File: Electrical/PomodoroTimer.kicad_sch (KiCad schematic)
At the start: 1 part

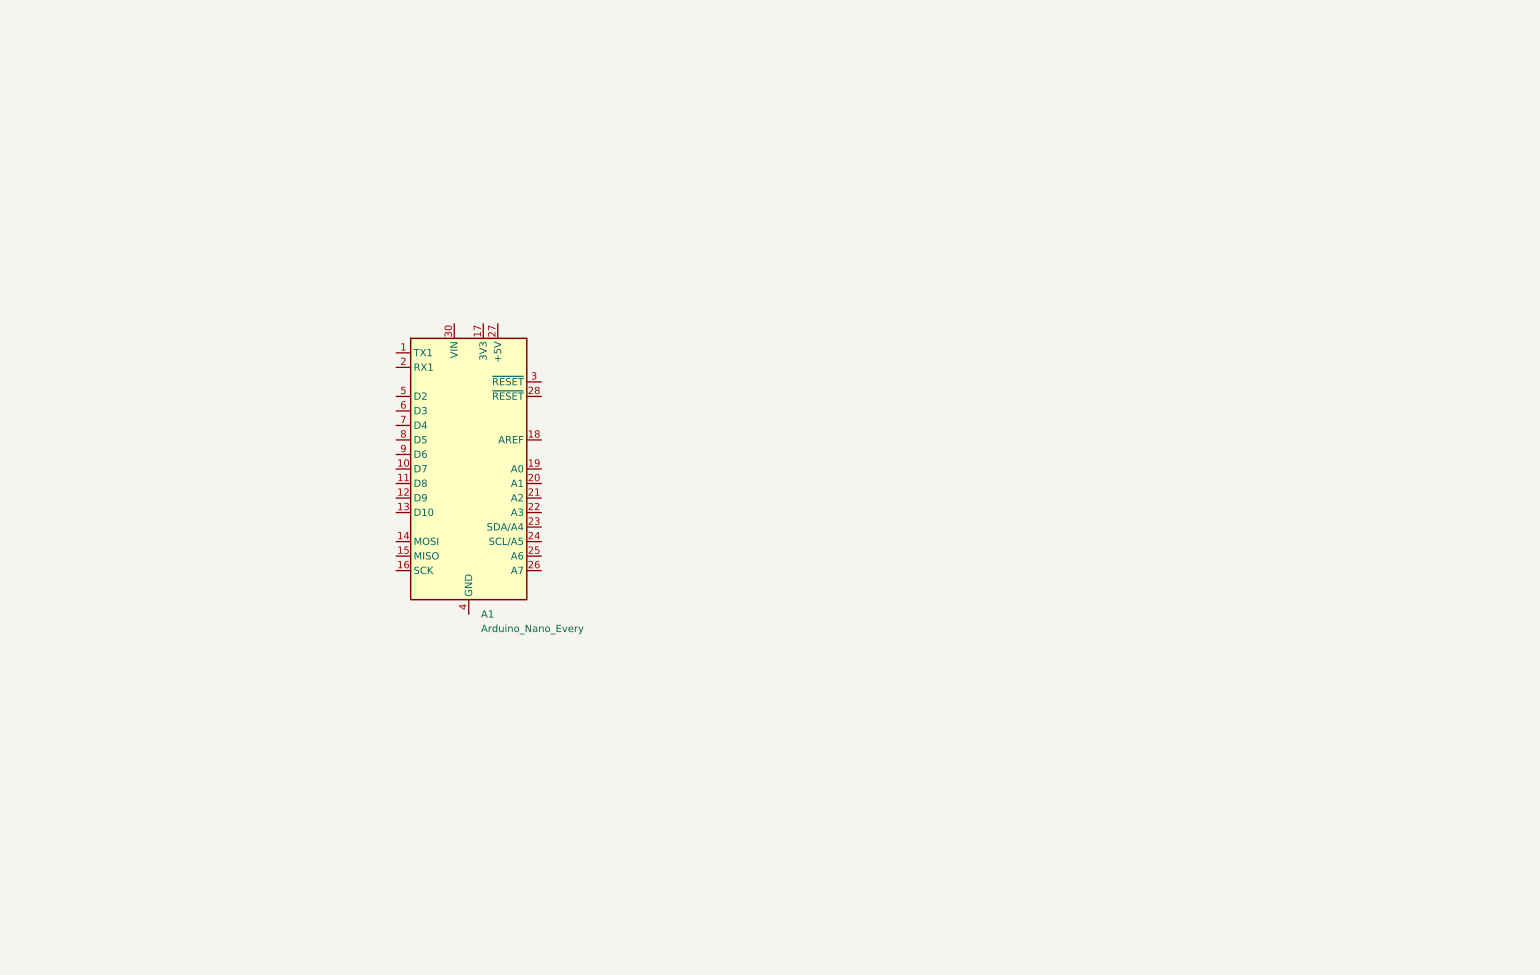
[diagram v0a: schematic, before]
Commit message: created schematic and pcb design for pomodoro timer
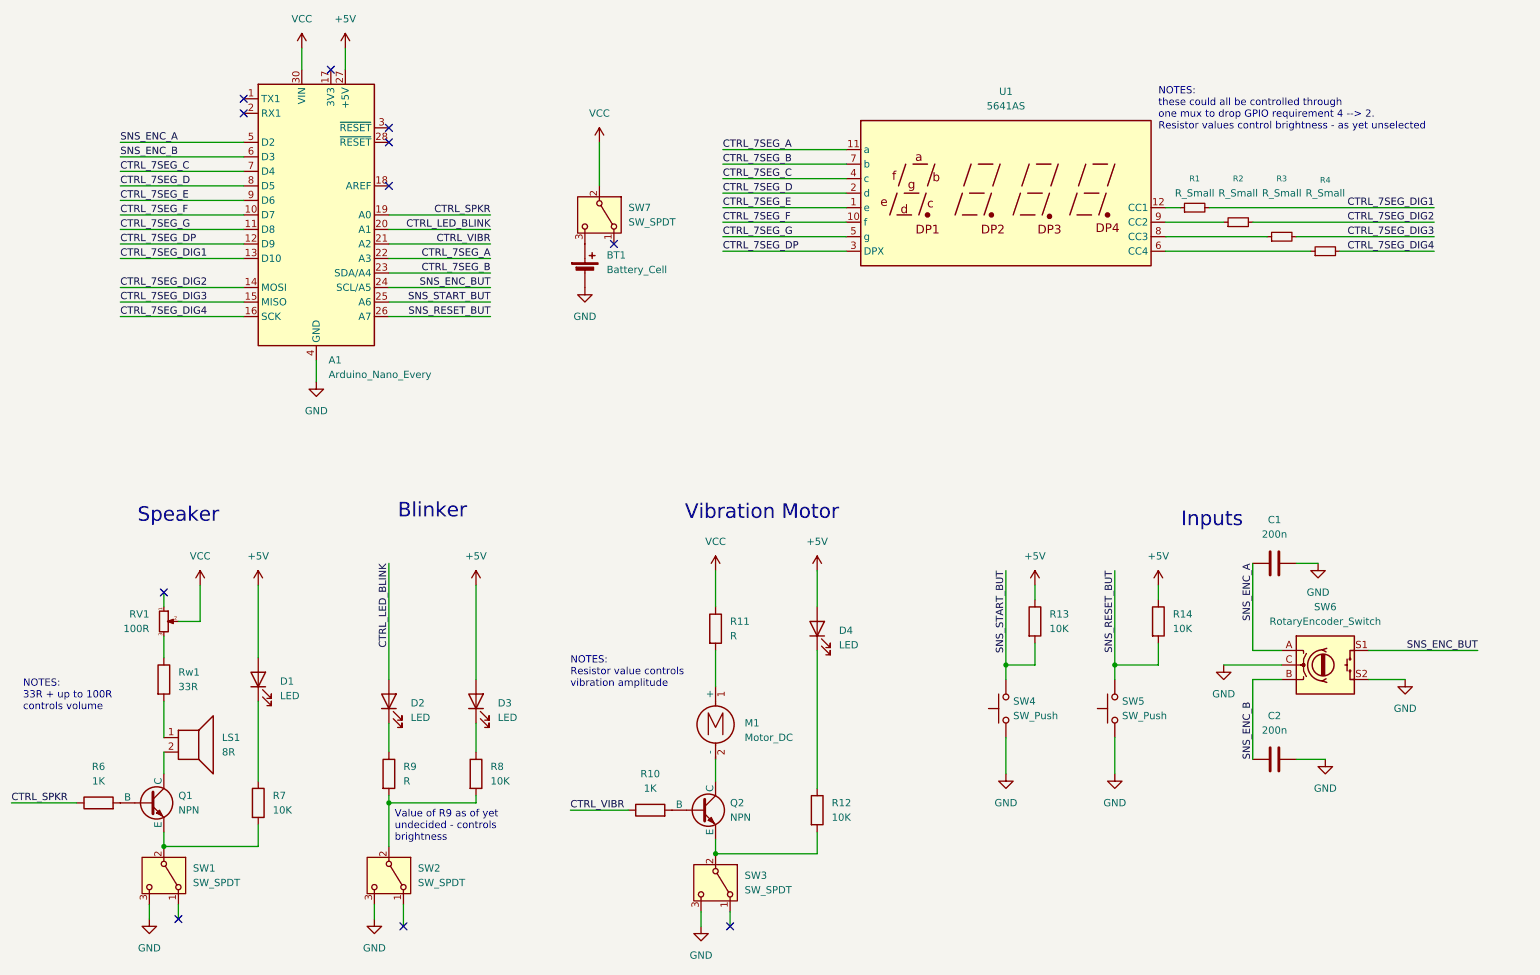
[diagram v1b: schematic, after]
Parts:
- added BT1: Battery_Cell, Connector_PinHeader_2.54mm:PinHeader_1x02_P2.54mm_Horizontal, symbol Device:Battery_Cell
- added C1, C2: 200n, Capacitor_THT:C_Axial_L3.8mm_D2.6mm_P10.00mm_Horizontal, symbol Device:C
- added D1, D2, D3, D4: LED, LED_THT:LED_D2.0mm_W4.8mm_H2.5mm_FlatTop, symbol Device:LED
- added LS1: 8R, Connector_PinHeader_2.54mm:PinHeader_1x02_P2.54mm_Horizontal, symbol Device:Speaker
- added M1: Motor_DC, Connector_PinHeader_2.54mm:PinHeader_1x02_P2.54mm_Horizontal, symbol Motor:Motor_DC
- added Q1, Q2: NPN, Connector_PinHeader_2.54mm:PinHeader_1x03_P2.54mm_Vertical, symbol Simulation_SPICE:NPN
- added R1, R2, R3, R4: R_Small, Resistor_THT:R_Axial_DIN0207_L6.3mm_D2.5mm_P10.16mm_Horizontal, symbol Device:R_Small
- added R10, R6: 1K, Resistor_THT:R_Axial_DIN0207_L6.3mm_D2.5mm_P10.16mm_Horizontal, symbol Device:R
- added R11, R9: R, Resistor_THT:R_Axial_DIN0207_L6.3mm_D2.5mm_P10.16mm_Horizontal, symbol Device:R
- added R12, R13, R14, R7, R8: 10K, Resistor_THT:R_Axial_DIN0207_L6.3mm_D2.5mm_P10.16mm_Horizontal, symbol Device:R
- added RV1: 100R, Connector_PinHeader_2.54mm:PinHeader_1x03_P2.54mm_Vertical, symbol Device:R_Potentiometer_Small
- added Rw1: 33R, Resistor_THT:R_Axial_DIN0207_L6.3mm_D2.5mm_P10.16mm_Horizontal, symbol Device:R
- added SW1, SW2, SW3, SW7: SW_SPDT, Connector_PinHeader_2.54mm:PinHeader_1x03_P2.54mm_Vertical, symbol Switch:SW_SPDT
- added SW4, SW5: SW_Push, Button_Switch_THT:SW_SPST_Omron_B3F-40xx, symbol Switch:SW_Push
- added SW6: RotaryEncoder_Switch, Rotary_Encoder:RotaryEncoder_Alps_EC11E-Switch_Vertical_H20mm, symbol Device:RotaryEncoder_Switch
- added U1: 5641AS, Display_7Segment:CA56-12SURKWA, symbol Display_Character:CC56-12SURKWA
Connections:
- net CTRL_7SEG_F: now reaches A1.10 (D7)
- net CTRL_7SEG_F: now also U1.10 (f)
- net CTRL_7SEG_G: now reaches A1.11 (D8)
- net CTRL_7SEG_G: now also U1.5 (g)
- net CTRL_7SEG_DP: now reaches A1.12 (D9)
- net CTRL_7SEG_DP: now also U1.3 (DPX)
- net CTRL_7SEG_DIG1: now reaches A1.13 (D10)
- net CTRL_7SEG_DIG1: now also R1.2
- net CTRL_7SEG_DIG2: now reaches A1.14 (MOSI)
- net CTRL_7SEG_DIG2: now also R2.2
- net CTRL_7SEG_DIG3: now reaches A1.15 (MISO)
- net CTRL_7SEG_DIG3: now also R3.2
- net CTRL_7SEG_DIG4: now reaches A1.16 (SCK)
- net CTRL_7SEG_DIG4: now also R4.2
- net CTRL_SPKR: now reaches A1.19 (A0)
- net CTRL_SPKR: now also R6.1
- net CTRL_LED_BLINK: now reaches A1.20 (A1)
- net CTRL_LED_BLINK: now also D2.2 (A)
- net CTRL_VIBR: now reaches A1.21 (A2)
- net CTRL_VIBR: now also R10.1
- net CTRL_7SEG_A: now reaches A1.22 (A3)
- net CTRL_7SEG_A: now also U1.11 (a)
- net CTRL_7SEG_B: now reaches A1.23 (SDA/A4)
- net CTRL_7SEG_B: now also U1.7 (b)
- net SNS_ENC_BUT: now reaches A1.24 (SCL/A5)
- net SNS_ENC_BUT: now also SW6.S1
- net SNS_START_BUT: now reaches A1.25 (A6)
- net SNS_START_BUT: now also R13.2, SW4.2
- net SNS_RESET_BUT: now reaches A1.26 (A7)
- net SNS_RESET_BUT: now also R14.2, SW5.2
- net +5V: now reaches A1.27 (+5V)
- net +5V: now also D1.2 (A), D3.2 (A), D4.2 (A), R13.1, R14.1
- net GND: now reaches A1.29 (GND), A1.4 (GND)
- net GND: now also BT1.2 (-), C1.2, C2.2, SW1.3 (C), SW2.3 (C), SW3.3 (C), SW4.1, SW5.1, SW6.C, SW6.S2
- net VCC: now reaches A1.30 (VIN)
- net VCC: now also R11.1, RV1.2, SW7.2 (B)
- net SNS_ENC_A: now reaches A1.5 (D2)
- net SNS_ENC_A: now also C1.1, SW6.A
- net SNS_ENC_B: now reaches A1.6 (D3)
- net SNS_ENC_B: now also C2.1, SW6.B
- net CTRL_7SEG_C: now reaches A1.7 (D4)
- net CTRL_7SEG_C: now also U1.4 (c)
- net CTRL_7SEG_D: now reaches A1.8 (D5)
- net CTRL_7SEG_D: now also U1.2 (d)
- net CTRL_7SEG_E: now reaches A1.9 (D6)
- net CTRL_7SEG_E: now also U1.1 (e)
- new net: R1.1, U1.12 (CC1)
- new net: LS1.1, Rw1.2
- new net: LS1.2, Q1.1 (C)
- new net: RV1.3, Rw1.1
- new net: BT1.1 (+), SW7.3 (C)
- new net: D1.1 (K), R7.1
- new net: Q1.3 (E), R7.2, SW1.2 (B)
- new net: R2.1, U1.9 (CC2)
- new net: R3.1, U1.8 (CC3)
- new net: D2.1 (K), R9.1
- new net: R8.2, R9.2, SW2.2 (B)
- new net: D4.1 (K), R12.1
- new net: Q2.3 (E), R12.2, SW3.2 (B)
- new net: M1.1 (+), R11.2
- new net: R4.1, U1.6 (CC4)
- new net: D3.1 (K), R8.1
- new net: Q1.2 (B), R6.2
- new net: M1.2 (-), Q2.1 (C)
- new net: Q2.2 (B), R10.2
- no-connect marks 0 -> 11
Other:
- note added: "Blinker"
- note added: "Inputs"
- note added: "NOTES: 33R + up to 100R controls volume"
- note added: "NOTES: Resistor value controls vibration amplitude"
- note added: "NOTES: these could all be controlled through one mux to drop GPIO requirement 4 --> 2. Resistor values control brightness - as yet unselected"
- note added: "Speaker"
- note added: "Value of R9 as of yet undecided - controls brightness"
- note added: "Vibration Motor"
- moved on the sheet: A1
